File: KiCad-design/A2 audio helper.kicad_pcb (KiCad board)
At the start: 2 copper layers, 45.5 x 85.5 mm, 42 parts, among them J1 PIN HEADER 1x2, J10 Conn_01x03, J11 SJ1-3515N, J12 PIN HEADER 1x5, J13 PIN HEADER 1x2, J14 PIN HEADER 1x2, J15 PIN HEADER 1x3, J16 PIN HEADER 1x3, J17 PIN HEADER 1x3, J18 PIN HEADER 2x6, J19 PIN HEADER 2x6, J2 PIN HEADER 1x2, J20 SJ1-3515N, J3 PIN HEADER 1x2, J4 SJ1-3515N, J5 PIN HEADER 1x3, J6 PIN HEADER 1x3, J7 Conn_01x03, J8 Conn_01x03, J9 Conn_01x03, K1 SR11-5V-200-2C, SW2 SW_DPDT_x2, U1 pam8403

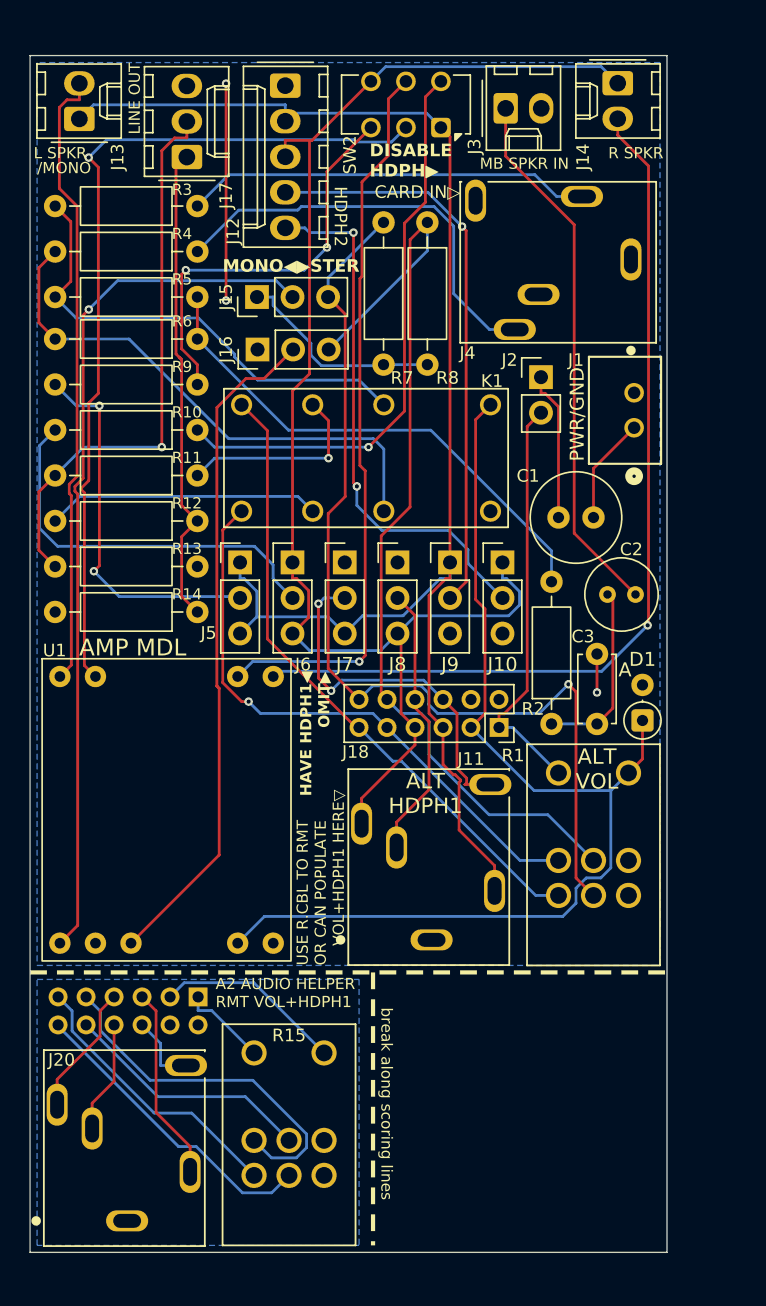
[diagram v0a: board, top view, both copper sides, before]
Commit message: improved fix for dual headphones
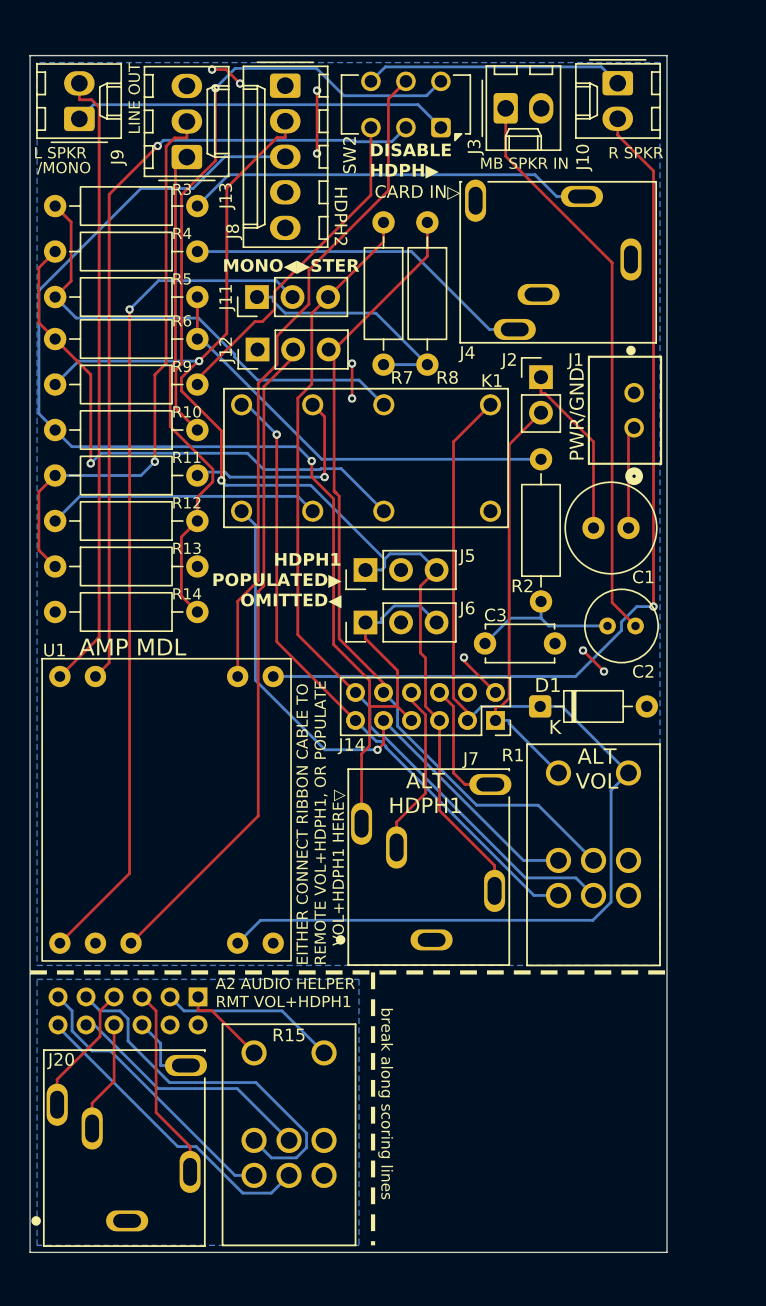
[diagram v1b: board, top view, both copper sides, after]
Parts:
- removed the J10 at (83.8, 71.2)
- removed the J7 at (72.5, 71.2)
- removed the J8 at (76.2, 71.2)
- removed the J9 at (80.0, 71.2)
- D1: footprint Diode_THT:D_DO-35_SOD27_P2.54mm_Vertical_AnodeUp -> Diode_THT:D_DO-35_SOD27_P7.62mm_Horizontal
- moved C3 9.85 mm to (82.5, 77.0), turned to 0 degrees
- moved J5 8.98 mm to (74.0, 71.8), turned to 90 degrees
- moved R2 8.78 mm to (86.5, 74.0)
- moved D1 7.38 mm to (86.4, 81.5), turned to 0 degrees
- moved J6 6.75 mm to (74.0, 75.5), turned to 90 degrees
- moved C1 2.61 mm to (92.8, 68.8)
- moved C2 2.25 mm to (93.2, 75.8)
- moved J14 0.56 mm to (83.2, 82.5)
- renumbered J14 to J10, J15 to J11, J16 to J12, J17 to J13, J18 to J14, J19 to J15, J11 to J7, J12 to J8, J13 to J9
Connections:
- J10 pad 1: HP1_R -> Net-(J10-Pin_1)
- J8 pad 4: Net-(J12-Pin_4) -> /HP2_TN
- J8 pad 5: Net-(J10-Pin_2) (its old number) -> /HP2_RN
- J9 pad 1: HP1_T -> Net-(J5-Pin_2)
- R10 pad 2: /HP_R -> HP1_R
- R9 pad 2: /HP_L -> HP1_T
- SW2 pad 1: HP1_T -> Net-(J5-Pin_2)
- SW2 pad 4: HP1_R -> Net-(J10-Pin_1)
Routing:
- net Net-(J12-Pin_4): track 40.8 -> 0.00 mm, vias 1 -> 0
- net Net-(J10-Pin_2) (its old number): track 38.3 -> 0.00 mm, vias 2 -> 0
- net /HP_R: track 28.2 -> 0.00 mm
- net /HP_L: track 27.0 -> 0.00 mm, vias 2 -> 0
- net Net-(J5-Pin_2): track 0.00 -> 26.9 mm
- net HP1_T: track 109.0 -> 87.2 mm, vias 0 -> 2
- net Net-(J10-Pin_1): track 0.00 -> 18.5 mm
- net HP1_TN: track 26.2 -> 9.14 mm, vias 2 -> 0
- net VOL_R: track 68.5 -> 59.2 mm
- net VOL_L: track 71.0 -> 61.6 mm, vias 1 -> 0
- net HP1_RN: track 19.7 -> 12.3 mm
- net HP1_R: track 101.9 -> 95.7 mm, vias 0 -> 1
- net /AUDIO_MB_AC: track 36.8 -> 31.1 mm
- net Net-(SW2A-C): track 29.4 -> 23.8 mm, vias 2 -> 0
- net /JACK_R: track 30.5 -> 25.0 mm
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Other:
- board text added: "EITHER CONNECT RIBBON CABLE TO REMOTE VOL+HDPH1, OR POPULATE VOL+HDPH1 HERE▽"
- board text added: "HDPH1 POPULATED▶ ︎OMITTED◀"
- board text removed: "HAVE HDPH1◀ ︎OMIT▶"
- board text removed: "USE R.CBL TO RMT OR CAN POPULATE VOL+HDPH1 HERE▽"

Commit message: tweaks to pcb, found vol knob 3dmodel
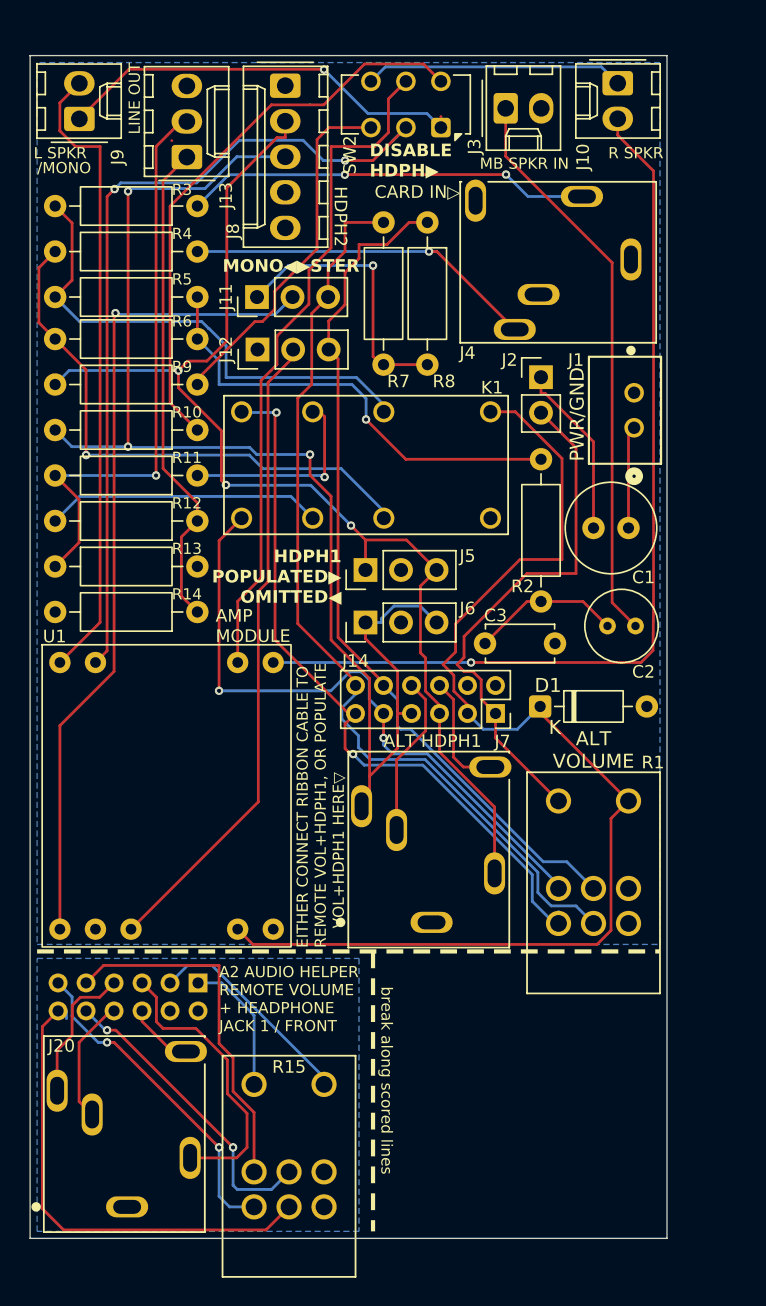
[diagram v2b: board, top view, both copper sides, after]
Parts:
- moved R15 2.25 mm to (68.5, 114.8)
- moved R1 2.00 mm to (90.2, 94.5)
- moved J7 1.25 mm to (78.7, 96.9)
- moved J15 1.00 mm to (62.0, 101.2)
- moved J20 1.00 mm to (56.9, 117.2)
- moved U1 1.00 mm to (59.8, 87.2)
- moved J14 0.50 mm to (83.2, 82.0)
- moved K1 0.50 mm to (74.0, 64.2)
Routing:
- net GND: track 15.0 -> 0.13 mm, vias 9 -> 0
- net /Daughterboard/REM_VOL_L: track 22.1 -> 34.7 mm
- net V_AMP: track 75.6 -> 85.0 mm
- net V_IN: track 29.7 -> 38.9 mm
- net SRC_L: track 45.9 -> 52.8 mm, vias 1 -> 2
- net /Daughterboard/RMT_HP1_T: track 13.9 -> 20.7 mm
- net VOL_L: track 61.6 -> 67.1 mm
- net SRC_R: track 42.2 -> 46.5 mm, vias 1 -> 2
- net /Daughterboard/REM_VOL_R: track 17.9 -> 21.9 mm, vias 0 -> 2
- net /Daughterboard/RMT_V_IN: track 6.23 -> 9.89 mm
- net /Daughterboard/RMT_SRC_L: track 20.1 -> 23.5 mm, vias 0 -> 2
- net Net-(SW2B-C): track 44.2 -> 40.9 mm, vias 1 -> 0
- net VOL_R: track 59.2 -> 62.3 mm
- net /MONO_MIX_POINT: track 17.5 -> 20.5 mm, vias 0 -> 1
- net Net-(J5-Pin_2): track 26.9 -> 29.8 mm, vias 0 -> 1
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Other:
- board size 45.5 x 85.5 mm -> 45.5 x 84.5 mm
- board text added: "A2 AUDIO HELPER REMOTE VOLUME + HEADPHONE JACK 1 / FRONT"
- board text added: "ALT VOLUME"
- board text added: "AMP MODULE"
- board text added: "Apple 2 Audio Helper v0.9.2"
- board text added: "break along scored lines"
- board text removed: "A2 AUDIO HELPER RMT VOL+HDPH1"
- board text removed: "ALT VOL"
- board text removed: "AMP MDL"
- board text removed: "Apple 2 Audio Helper v0.8"
- board text removed: "break along scoring lines"

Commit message: made power & speaker input connectors also horizontal
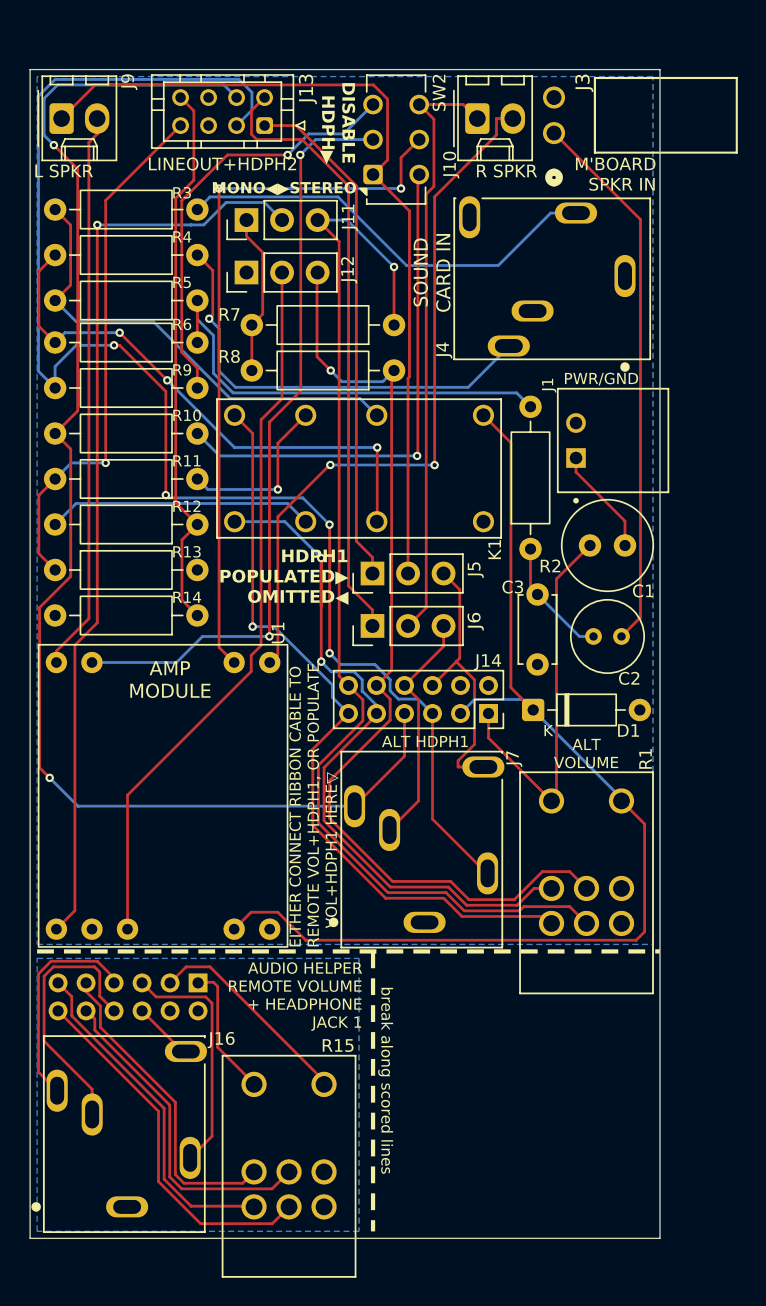
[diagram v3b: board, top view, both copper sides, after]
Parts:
- removed J2: PIN HEADER 1x2, Connector_PinHeader_2.54mm:PinHeader_1x02_P2.54mm_Vertical
- removed J8: PIN HEADER 1x5, Connector_Molex:Molex_KK-254_AE-6410-05A_1x05_P2.54mm_Vertical
- J1: footprint Molex5267:CONN_22035025_MOL -> Molex 22-05-7025:MOLEX_22-05-7025
- J13: value PIN HEADER 1x3 -> PIN HEADER 2x4; footprint Connector_Molex:Molex_KK-254_AE-6410-03A_1x03_P2.54mm_Vertical -> Connector_JST:JST_PHD_B8B-PHDSS_2x04_P2.00mm_Vertical
- J3: footprint Connector_Molex:Molex_KK-254_AE-6410-02A_1x02_P2.54mm_Vertical -> Molex 22053021:CONN_A-7478-02A_MOL
- moved R8 10.8 mm to (76.0, 57.5), turned to 180 degrees
- moved J10 10.3 mm to (82.0, 39.5), turned to 0 degrees
- moved R7 7.37 mm to (76.0, 54.2), turned to 180 degrees
- moved J13 5.99 mm to (66.8, 40.0), turned to 180 degrees
- moved SW2 5.90 mm to (74.5, 43.5), turned to 90 degrees
- moved J12 5.56 mm to (65.5, 50.5)
- moved J11 5.55 mm to (65.5, 46.8)
- moved C3 5.13 mm to (86.2, 73.5), turned to -90 degrees
- moved J1 4.25 mm to (89.0, 62.5), turned to 90 degrees
- moved J3 3.88 mm to (87.4, 40.5), turned to 90 degrees
- moved R2 3.82 mm to (85.8, 70.2)
- moved C1 1.27 mm to (92.5, 70.0)
- moved J9 1.27 mm to (52.2, 39.5), turned to 0 degrees
- moved J4 1.26 mm to (92.5, 50.8)
- moved C2 1.25 mm to (92.2, 76.5)
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- renumbered J20 to J16
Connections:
- net /LINE_OUT_SOURCE_L renamed /LINEOUT_SOURCE_L
- net /LINE_OUT_SOURCE_R renamed /LINEOUT_SOURCE_R
- net /MONO_MIX_POINT renamed /MONO_MIX
- C1 pad 2: Net-(J2-Pin_1) -> V_IN
- J10 pad 1: Net-(J10-Pin_1) -> /SPKR_R
- J13 pad 1: /LINE_OUT_L -> /HP2_TN
- J13 pad 2: /LINE_OUT_R -> /HP2_RN
- J13 pad 3: GND -> HP1_T
- J5 pad 1: HP1_T -> /HP2_TN
- J5 pad 2: /HP_L -> /SPKR_L
- J5 pad 3: HP1_T -> HP1_TN
- J6 pad 1: HP1_R -> /HP2_RN
- J6 pad 2: /HP_R -> /SPKR_R
- J6 pad 3: HP1_R -> HP1_RN
- J9 pad 1: Net-(J5-Pin_2) -> /SPKR_L
- R11 pad 2: /LINE_OUT_R -> /LINEOUT_L
- R12 pad 1: /LINE_OUT_L -> /LINEOUT_R
- R13 pad 1: /LINE_OUT_R -> /LINEOUT_L
- R14 pad 1: /LINE_OUT_L -> /LINEOUT_R
- SW2 pad 1: Net-(J5-Pin_2) -> /SPKR_L
- SW2 pad 4: Net-(J10-Pin_1) -> /SPKR_R
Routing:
- net /SPKR_L: track 0.00 -> 60.1 mm
- net /HP2_RN: track 0.00 -> 43.6 mm
- net /SPKR_R: track 0.00 -> 43.0 mm
- net /LINE_OUT_R: track 41.6 -> 0.00 mm, vias 1 -> 0
- net /LINEOUT_R: track 0.00 -> 39.5 mm
- net /LINEOUT_L: track 0.00 -> 37.9 mm, vias 0 -> 1
- net /HP2_TN: track 0.00 -> 36.5 mm
- net /LINE_OUT_L: track 35.2 -> 0.00 mm
- net Net-(J5-Pin_2): track 29.8 -> 0.00 mm, vias 1 -> 0
- net HP1_T: track 85.0 -> 103.9 mm, vias 3 -> 4
- net Net-(J10-Pin_1): track 18.5 -> 0.00 mm
- net Net-(J10-Pin_2): track 66.9 -> 51.0 mm, vias 1 -> 2
- net Net-(J2-Pin_1): track 12.5 -> 0.00 mm
- net VOL_L: track 67.1 -> 79.1 mm, vias 0 -> 1
- net V_IN: track 38.9 -> 27.5 mm
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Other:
- board size 45.5 x 84.5 mm -> 45 x 83.5 mm
- board text added: "AUDIO HELPER REMOTE VOLUME + HEADPHONE JACK 1"
- board text added: "Apple 2 Audio Helper v0.10"
- board text added: "LINEOUT+HDPH2"
- board text added: "M'BOARD SPKR IN"
- board text added: "MONO◀︎▶︎STEREO"
- board text added: "SOUND CARD IN"
- board text removed: "/MONO"
- board text removed: "A2 AUDIO HELPER REMOTE VOLUME + HEADPHONE JACK 1 / FRONT"
- board text removed: "Apple 2 Audio Helper v0.9.2"
- board text removed: "CARD IN▷"
- board text removed: "HDPH2"
- board text removed: "LINE OUT"
- board text removed: "MB SPKR IN"
- board text removed: "MONO◀︎▶︎STER"

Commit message: added recommended decoupling cap to amp pwr/gnd
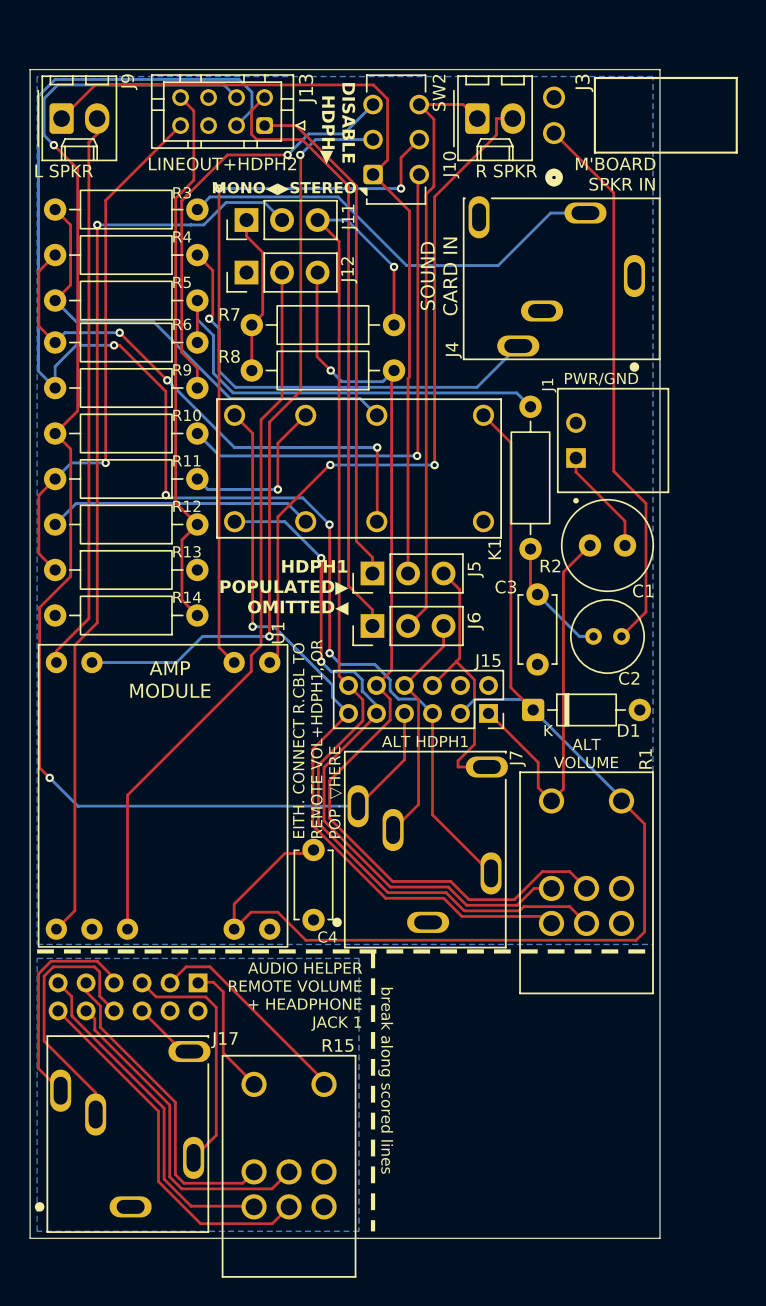
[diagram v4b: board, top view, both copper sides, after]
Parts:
- added C4: 100nF, Capacitor_THT:C_Disc_D4.7mm_W2.5mm_P5.00mm, F.Cu at (70.2, 91.8)
- moved J4 0.67 mm to (93.2, 50.8)
- moved J17 0.25 mm to (57.2, 117.2)
- moved J7 0.25 mm to (78.4, 96.9)
- renumbered J14 to J15, J15 to J16, J16 to J17
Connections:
- net GND2 renamed RMT_GND
- J10 pad 2: Net-(J10-Pin_2) -> /SPKR_R
- J9 pad 2: Net-(J9-Pin_2) -> /SPKR_L
- U1 pad 6: Net-(J10-Pin_2) -> /SPKR_R
- U1 pad 9: Net-(J9-Pin_2) -> /SPKR_L
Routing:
- net /SPKR_R: track 43.0 -> 94.0 mm, vias 0 -> 2
- net Net-(J10-Pin_2): track 51.0 -> 0.00 mm, vias 2 -> 0
- net Net-(J9-Pin_2): track 40.1 -> 0.00 mm
- net /SPKR_L: track 60.1 -> 100.2 mm
- net V_AMP: track 78.5 -> 87.4 mm
- net /JACK_R: track 31.6 -> 32.3 mm
- net /JACK_L: track 31.0 -> 31.7 mm
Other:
- board text added: "Apple 2 Audio Helper v0.10.3"
- board text added: "EITH. CONNECT R.CBL TO REMOTE VOL+HDPH1, OR POP. ▽HERE"
- board text removed: "Apple 2 Audio Helper v0.10"
- board text removed: "EITHER CONNECT RIBBON CABLE TO REMOTE VOL+HDPH1, OR POPULATE VOL+HDPH1 HERE▽"

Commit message: changed pwr/gnd connector to more common jst connector
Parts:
- J1: footprint Molex 22-05-7025:MOLEX_22-05-7025 -> Connector_JST:JST_XH_S2B-XH-A_1x02_P2.50mm_Horizontal
- moved R2 7.58 mm to (85.8, 77.8)
- moved C3 7.16 mm to (87.8, 80.5), turned to 0 degrees
- moved J1 2.25 mm to (86.8, 63.0)
- moved D1 1.77 mm to (85.7, 83.5)
- moved C2 0.75 mm to (92.2, 75.8)
- moved R7 0.67 mm to (75.3, 54.2)
- moved R8 0.67 mm to (75.3, 57.5)
- moved C1 0.50 mm to (92.5, 69.5)
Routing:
- net V_AMP: track 87.4 -> 95.5 mm, vias 0 -> 1
- net /AUDIO_MB_AC: track 32.3 -> 38.7 mm
- net SRC_R: track 52.9 -> 49.3 mm
- net /AMP_INPUT_L: track 65.9 -> 63.0 mm
- net Net-(SW2B-B): track 51.3 -> 48.5 mm
- net SRC_L: track 54.6 -> 57.0 mm
- net /SPKR_R: track 94.0 -> 95.2 mm
- net /+5V_IN: track 7.70 -> 8.86 mm
- net /HP2_TN: track 36.5 -> 37.4 mm
- net /HP2_RN: track 43.6 -> 44.5 mm
- net Net-(SW2A-B): track 54.4 -> 55.3 mm, vias 2 -> 1
- net /MB_SPKR: track 39.4 -> 38.7 mm
- net /JACK_R: track 32.3 -> 32.8 mm
- net /LINEOUT_SOURCE_L: track 12.2 -> 12.7 mm
- net HP1_T: track 104.0 -> 104.5 mm
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
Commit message: fixed mb spkr pin 2 which isnt ground afterall
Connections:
- J3 pad 2: GND -> unconnected-(J3-Pin_2-Pad2)
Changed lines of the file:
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@@
 		(title "Apple 2 Audio Helper")
 		(date "2026-02-18")
-		(rev "0.10.4")
+		(rev "0.10.5")
 		(company "Northwest Retroventures")
 		(comment 1 "Optionally supports second internal speaker for stereo.")
@@
 	(net 47 "unconnected-(J15-Pin_4-Pad4)")
 	(net 48 "/LINEOUT_SOURCE_L")
+	(net 49 "unconnected-(J3-Pin_2-Pad2)")
 	(footprint "Capacitor_THT:C_Disc_D4.7mm_W2.5mm_P5.00mm"
 		(layer "F.Cu")
@@
 			(layers "*.Cu" "*.Mask")
 			(remove_unused_layers no)
-			(net 26 "GND")
+			(net 49 "unconnected-(J3-Pin_2-Pad2)")
 			(pinfunction "Pin_2")
-			(pintype "passive")
+			(pintype "passive+no_connect")
 			(solder_mask_margin 0.102)
 		)
